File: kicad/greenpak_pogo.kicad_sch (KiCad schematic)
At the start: 5 parts, among them J1 JST_SH_SM04B-SRSS-TB_1x04-1MP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, J2 GREENPAK_POGO_PINS

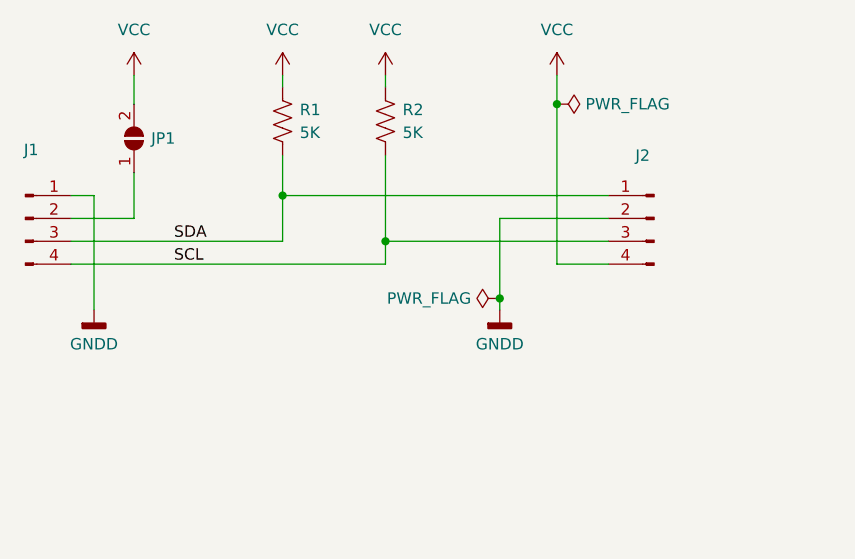
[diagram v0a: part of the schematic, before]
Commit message: Added schematic to the doc.
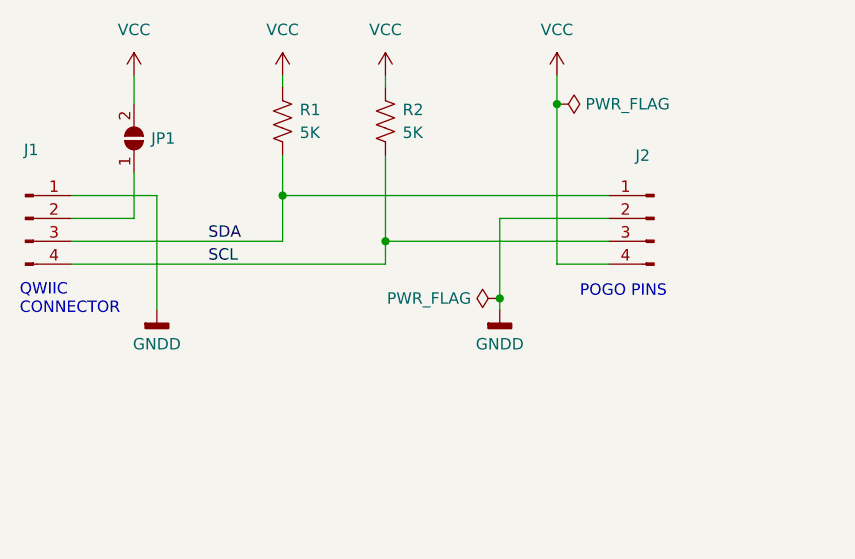
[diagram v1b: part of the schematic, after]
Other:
- note added: "POGO PINS"
- note added: "QWIIC CONNECTOR"
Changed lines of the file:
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@@
     (stroke (width 0) (type default))
   )
-  (wire (pts (xy 132.715 100.965) (xy 109.22 100.965))
+  (wire (pts (xy 109.22 100.965) (xy 132.715 100.965))
     (stroke (width 0) (type default))
   )
@@
     (stroke (width 0) (type default))
   )
-  (wire (pts (xy 109.22 95.885) (xy 111.76 95.885))
+  (wire (pts (xy 109.22 95.885) (xy 118.745 95.885))
     (stroke (width 0) (type default))
   )
@@
     (stroke (width 0) (type default))
   )
-  (wire (pts (xy 111.76 95.885) (xy 111.76 108.585))
+  (wire (pts (xy 118.745 95.885) (xy 118.745 108.585))
     (stroke (width 0) (type default))
   )
@@
     (effects (font (size 1.27 1.27)) (justify left bottom))
   )
-  (label "SDA" (at 120.65 100.965 0) (fields_autoplaced)
-    (effects (font (size 1.27 1.27)) (justify left bottom))
-  )
-  (label "SCL" (at 120.65 103.505 0) (fields_autoplaced)
+  (text "QWIIC\nCONNECTOR" (at 103.505 109.22 0)
+    (effects (font (size 1.27 1.27)) (justify left bottom))
+  )
+  (text "POGO PINS" (at 165.735 107.315 0)
+    (effects (font (size 1.27 1.27)) (justify left bottom))
+  )
+  (label "SDA" (at 124.46 100.965 0) (fields_autoplaced)
+    (effects (font (size 1.27 1.27)) (justify left bottom))
+  )
+  (label "SCL" (at 124.46 103.505 0) (fields_autoplaced)
     (effects (font (size 1.27 1.27)) (justify left bottom))
   )
@@
     )
   )
-  (symbol (lib_id "power:GNDD") (at 111.76 108.585 0) (unit 1)
-    (in_bom yes) (on_board yes) (dnp no) (fields_autoplaced)
-    (property "Reference" "#PWR01" (at 111.76 114.935 0)
-      (effects (font (size 1.27 1.27)) hide)
-    )
-    (property "Value" "GNDD" (at 111.76 112.395 0)
-      (effects (font (size 1.27 1.27)))
-    )
-    (property "Footprint" "" (at 111.76 108.585 0)
-      (effects (font (size 1.27 1.27)) hide)
-    )
-    (property "Datasheet" "" (at 111.76 108.585 0)
-      (effects (font (size 1.27 1.27)) hide)
-    )
+  (symbol (lib_id "power:GNDD") (at 118.745 108.585 0) (unit 1)
+    (in_bom yes) (on_board yes) (dnp no) (fields_autoplaced)
+    (property "Reference" "#PWR01" (at 118.745 114.935 0)
+      (effects (font (size 1.27 1.27)) hide)
+    )
+    (property "Value" "GNDD" (at 118.745 112.395 0)
+      (effects (font (size 1.27 1.27)))
+    )
+    (property "Footprint" "" (at 118.745 108.585 0)
+      (effects (font (size 1.27 1.27)) hide)
+    )
+    (property "Datasheet" "" (at 118.745 108.585 0)
+      (effects (font (size 1.27 1.27)) hide)
+    )
